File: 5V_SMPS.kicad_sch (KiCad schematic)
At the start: 13 parts, among them U3 TS30041

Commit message: V3 2. Update ready for check
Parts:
- renumbered C5 to C44, C6 to C45, C15 to C46, C16 to C47, C17 to C48, D7 to D16, L1 to L3, R17 to R43, R18 to R44, R19 to R45, R20 to R46, R21 to R47, U3 to U13
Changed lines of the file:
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@@
   (symbol (lib_id "Device:R_Small") (at 202.565 75.565 0)
     (in_bom yes) (on_board yes)
-    (property "Reference" "R21" (id 0) (at 203.835 74.295 0)
+    (property "Reference" "R47" (id 0) (at 203.835 74.295 0)
       (effects (font (size 1.27 1.27)) (justify left))
     )
@@
   (symbol (lib_id "Device:C") (at 111.76 72.39 180)
     (in_bom yes) (on_board yes)
-    (property "Reference" "C5" (id 0) (at 114.3 69.85 0))
+    (property "Reference" "C44" (id 0) (at 114.3 69.85 0))
     (property "Value" "22u" (id 1) (at 114.3 74.93 0))
     (property "Footprint" "Capacitor_SMD:C_0805_2012Metric" (id 2) (at 110.7948 68.58 0)
@@
   (symbol (lib_id "Device:L") (at 170.815 57.785 90)
     (in_bom yes) (on_board yes)
-    (property "Reference" "L1" (id 0) (at 170.815 52.959 90))
+    (property "Reference" "L3" (id 0) (at 170.815 52.959 90))
     (property "Value" "4.7u" (id 1) (at 170.815 55.2704 90))
     (property "Footprint" "TXV_Library_Footprints:SRN4018TA-4R7M" (id 2) (at 170.815 57.785 0)
@@
   (symbol (lib_id "Device:C") (at 187.325 75.565 180)
     (in_bom yes) (on_board yes)
-    (property "Reference" "C17" (id 0) (at 189.865 73.025 0))
+    (property "Reference" "C48" (id 0) (at 189.865 73.025 0))
     (property "Value" "22u" (id 1) (at 188.595 78.105 0))
     (property "Footprint" "Capacitor_SMD:C_0805_2012Metric" (id 2) (at 186.3598 71.755 0)
@@
   (symbol (lib_id "Device:LED_Small_Filled") (at 194.31 75.565 90)
     (in_bom yes) (on_board yes)
-    (property "Reference" "D7" (id 0) (at 196.85 74.295 90))
+    (property "Reference" "D16" (id 0) (at 196.85 74.295 90))
     (property "Value" "5V" (id 1) (at 196.85 76.835 90))
     (property "Footprint" "LED_SMD:LED_0603_1608Metric" (id 2) (at 194.31 75.565 90)
@@
   (symbol (lib_id "Device:C") (at 180.975 75.565 180)
     (in_bom yes) (on_board yes)
-    (property "Reference" "C16" (id 0) (at 183.515 73.025 0))
+    (property "Reference" "C47" (id 0) (at 183.515 73.025 0))
     (property "Value" "22u" (id 1) (at 182.88 78.105 0))
     (property "Footprint" "Capacitor_SMD:C_0805_2012Metric" (id 2) (at 180.0098 71.755 0)
@@
   (symbol (lib_id "Device:R_Small") (at 194.31 66.675 0)
     (in_bom yes) (on_board yes)
-    (property "Reference" "R19" (id 0) (at 199.39 65.405 0)
+    (property "Reference" "R45" (id 0) (at 199.39 65.405 0)
       (effects (font (size 1.27 1.27)) (justify right))
     )
@@
   (symbol (lib_id "Device:R") (at 175.895 80.645 0)
     (in_bom yes) (on_board yes)
-    (property "Reference" "R18" (id 0) (at 170.815 80.01 0)
+    (property "Reference" "R44" (id 0) (at 170.815 80.01 0)
       (effects (font (size 1.27 1.27)) (justify left))
     )
@@
   (symbol (lib_id "Device:R_Small") (at 202.565 66.675 0)
     (in_bom yes) (on_board yes)
-    (property "Reference" "R20" (id 0) (at 203.835 65.405 0)
+    (property "Reference" "R46" (id 0) (at 203.835 65.405 0)
       (effects (font (size 1.27 1.27)) (justify left))
     )
@@
   (symbol (lib_id "Device:R") (at 175.895 69.215 180)
     (in_bom yes) (on_board yes)
-    (property "Reference" "R17" (id 0) (at 172.72 68.58 0))
+    (property "Reference" "R43" (id 0) (at 172.72 68.58 0))
     (property "Value" "R" (id 1) (at 175.895 67.945 90))
     (property "Footprint" "Resistor_SMD:R_0603_1608Metric" (id 2) (at 177.673 69.215 90)
@@
   (symbol (lib_id "TXV_Library_Symbols:TS30041") (at 140.335 69.215 0)
     (in_bom yes) (on_board yes)
-    (property "Reference" "U3" (id 0) (at 140.335 51.054 0))
+    (property "Reference" "U13" (id 0) (at 140.335 51.054 0))
     (property "Value" "TS30041" (id 1) (at 140.335 53.3654 0))
     (property "Footprint" "Package_DFN_QFN:QFN-16-1EP_3x3mm_P0.5mm_EP1.75x1.75mm_ThermalVias" (id 2) (at 139.065 98.425 0)
@@
   (symbol (lib_id "Device:C") (at 160.655 57.785 270)
     (in_bom yes) (on_board yes)
-    (property "Reference" "C15" (id 0) (at 160.655 51.3842 90))
+    (property "Reference" "C46" (id 0) (at 160.655 51.3842 90))
     (property "Value" "100n" (id 1) (at 160.655 53.6956 90))
     (property "Footprint" "Capacitor_SMD:C_0402_1005Metric" (id 2) (at 156.845 58.7502 0)
@@
   (symbol (lib_id "Device:C") (at 118.745 72.39 0)
     (in_bom yes) (on_board yes)
-    (property "Reference" "C6" (id 0) (at 121.285 69.85 0))
+    (property "Reference" "C45" (id 0) (at 121.285 69.85 0))
     (property "Value" "100n" (id 1) (at 121.92 74.93 0))
     (property "Footprint" "Capacitor_SMD:C_0402_1005Metric" (id 2) (at 119.7102 76.2 0)

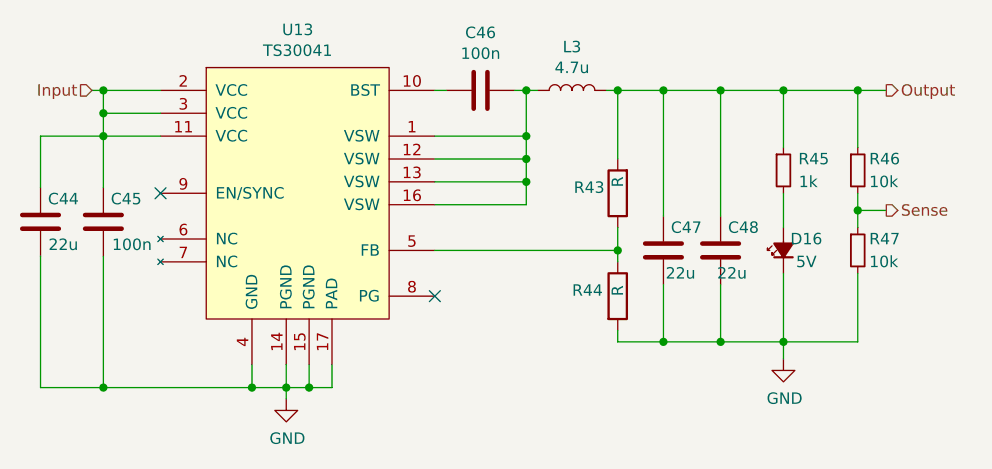
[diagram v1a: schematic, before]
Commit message: Schematic: Changed Polarity of umbilical connectors Schematic: Added TVS diode to battery_sense Schematic: Some minor prettyfication
Still wrong: Main LiIon Charger Enable connect to STM32
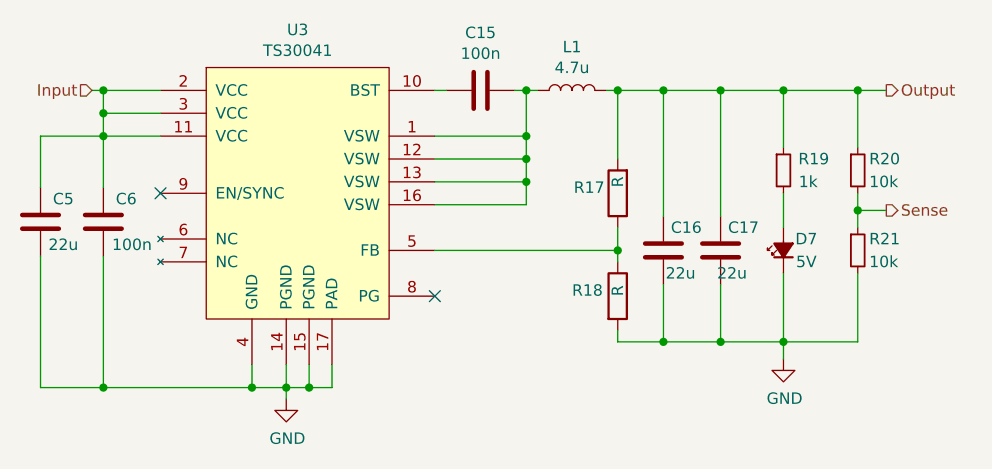
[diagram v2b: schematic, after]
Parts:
- renumbered C46 to C15, C47 to C16, C48 to C17, C44 to C5, C45 to C6, D16 to D7, L3 to L1, R43 to R17, R44 to R18, R45 to R19, R46 to R20, R47 to R21, U13 to U3
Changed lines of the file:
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@@
     (effects (font (size 1.27 1.27)) (justify right))
   )
-  (symbol (lib_id "Device:R_Small") (at 202.565 75.565 0)
-    (in_bom yes) (on_board yes)
-    (property "Reference" "R47" (id 0) (at 203.835 74.295 0)
+  (symbol (lib_id "Device:R_Small") (at 202.565 75.565 0) (unit 1)
+    (in_bom yes) (on_board yes)
+    (property "Reference" "R21" (id 0) (at 203.835 74.295 0)
       (effects (font (size 1.27 1.27)) (justify left))
     )
@@
     (pin "2")
   )
-  (symbol (lib_id "Device:C") (at 111.76 72.39 180)
-    (in_bom yes) (on_board yes)
-    (property "Reference" "C44" (id 0) (at 114.3 69.85 0))
+  (symbol (lib_id "Device:C") (at 111.76 72.39 180) (unit 1)
+    (in_bom yes) (on_board yes)
+    (property "Reference" "C5" (id 0) (at 114.3 69.85 0))
     (property "Value" "22u" (id 1) (at 114.3 74.93 0))
     (property "Footprint" "Capacitor_SMD:C_0805_2012Metric" (id 2) (at 110.7948 68.58 0)
@@
     (pin "2")
   )
-  (symbol (lib_id "Device:L") (at 170.815 57.785 90)
-    (in_bom yes) (on_board yes)
-    (property "Reference" "L3" (id 0) (at 170.815 52.959 90))
+  (symbol (lib_id "Device:L") (at 170.815 57.785 90) (unit 1)
+    (in_bom yes) (on_board yes)
+    (property "Reference" "L1" (id 0) (at 170.815 52.959 90))
     (property "Value" "4.7u" (id 1) (at 170.815 55.2704 90))
     (property "Footprint" "TXV_Library_Footprints:SRN4018TA-4R7M" (id 2) (at 170.815 57.785 0)
@@
     (pin "2")
   )
-  (symbol (lib_id "Device:C") (at 187.325 75.565 180)
-    (in_bom yes) (on_board yes)
-    (property "Reference" "C48" (id 0) (at 189.865 73.025 0))
+  (symbol (lib_id "Device:C") (at 187.325 75.565 180) (unit 1)
+    (in_bom yes) (on_board yes)
+    (property "Reference" "C17" (id 0) (at 189.865 73.025 0))
     (property "Value" "22u" (id 1) (at 188.595 78.105 0))
     (property "Footprint" "Capacitor_SMD:C_0805_2012Metric" (id 2) (at 186.3598 71.755 0)
@@
     (pin "2")
   )
-  (symbol (lib_id "Device:LED_Small_Filled") (at 194.31 75.565 90)
-    (in_bom yes) (on_board yes)
-    (property "Reference" "D16" (id 0) (at 196.85 74.295 90))
+  (symbol (lib_id "Device:LED_Small_Filled") (at 194.31 75.565 90) (unit 1)
+    (in_bom yes) (on_board yes)
+    (property "Reference" "D7" (id 0) (at 196.85 74.295 90))
     (property "Value" "5V" (id 1) (at 196.85 76.835 90))
     (property "Footprint" "LED_SMD:LED_0603_1608Metric" (id 2) (at 194.31 75.565 90)
@@
     (pin "2")
   )
-  (symbol (lib_id "power:GND") (at 139.065 92.075 0)
-    (in_bom yes) (on_board yes)
-    (property "Reference" "#PWR0102" (id 0) (at 139.065 98.425 0)
+  (symbol (lib_id "power:GND") (at 139.065 92.075 0) (unit 1)
+    (in_bom yes) (on_board yes)
+    (property "Reference" "#PWR093" (id 0) (at 139.065 98.425 0)
       (effects (font (size 1.27 1.27)) hide)
     )
@@
     (pin "1")
   )
-  (symbol (lib_id "Device:C") (at 180.975 75.565 180)
-    (in_bom yes) (on_board yes)
-    (property "Reference" "C47" (id 0) (at 183.515 73.025 0))
+  (symbol (lib_id "Device:C") (at 180.975 75.565 180) (unit 1)
+    (in_bom yes) (on_board yes)
+    (property "Reference" "C16" (id 0) (at 183.515 73.025 0))
     (property "Value" "22u" (id 1) (at 182.88 78.105 0))
     (property "Footprint" "Capacitor_SMD:C_0805_2012Metric" (id 2) (at 180.0098 71.755 0)
@@
     (pin "2")
   )
-  (symbol (lib_id "Device:R_Small") (at 194.31 66.675 0)
-    (in_bom yes) (on_board yes)
-    (property "Reference" "R45" (id 0) (at 199.39 65.405 0)
+  (symbol (lib_id "Device:R_Small") (at 194.31 66.675 0) (unit 1)
+    (in_bom yes) (on_board yes)
+    (property "Reference" "R19" (id 0) (at 199.39 65.405 0)
       (effects (font (size 1.27 1.27)) (justify right))
     )
@@
     (pin "2")
   )
-  (symbol (lib_id "power:GND") (at 194.31 87.63 0)
-    (in_bom yes) (on_board yes)
-    (property "Reference" "#PWR0103" (id 0) (at 194.31 93.98 0)
+  (symbol (lib_id "power:GND") (at 194.31 87.63 0) (unit 1)
+    (in_bom yes) (on_board yes)
+    (property "Reference" "#PWR0101" (id 0) (at 194.31 93.98 0)
       (effects (font (size 1.27 1.27)) hide)
     )
@@
     (pin "1")
   )
-  (symbol (lib_id "Device:R") (at 175.895 80.645 0)
-    (in_bom yes) (on_board yes)
-    (property "Reference" "R44" (id 0) (at 170.815 80.01 0)
+  (symbol (lib_id "Device:R") (at 175.895 80.645 0) (unit 1)
+    (in_bom yes) (on_board yes)
+    (property "Reference" "R18" (id 0) (at 170.815 80.01 0)
       (effects (font (size 1.27 1.27)) (justify left))
     )
@@
     (pin "2")
   )
-  (symbol (lib_id "Device:R_Small") (at 202.565 66.675 0)
-    (in_bom yes) (on_board yes)
-    (property "Reference" "R46" (id 0) (at 203.835 65.405 0)
+  (symbol (lib_id "Device:R_Small") (at 202.565 66.675 0) (unit 1)
+    (in_bom yes) (on_board yes)
+    (property "Reference" "R20" (id 0) (at 203.835 65.405 0)
       (effects (font (size 1.27 1.27)) (justify left))
     )
@@
     (pin "2")
   )
-  (symbol (lib_id "Device:R") (at 175.895 69.215 180)
-    (in_bom yes) (on_board yes)
-    (property "Reference" "R43" (id 0) (at 172.72 68.58 0))
+  (symbol (lib_id "Device:R") (at 175.895 69.215 180) (unit 1)
+    (in_bom yes) (on_board yes)
+    (property "Reference" "R17" (id 0) (at 172.72 68.58 0))
     (property "Value" "R" (id 1) (at 175.895 67.945 90))
     (property "Footprint" "Resistor_SMD:R_0603_1608Metric" (id 2) (at 177.673 69.215 90)
@@
     (pin "2")
   )
-  (symbol (lib_id "TXV_Library_Symbols:TS30041") (at 140.335 69.215 0)
-    (in_bom yes) (on_board yes)
-    (property "Reference" "U13" (id 0) (at 140.335 51.054 0))
+  (symbol (lib_id "TXV_Library_Symbols:TS30041") (at 140.335 69.215 0) (unit 1)
+    (in_bom yes) (on_board yes)
+    (property "Reference" "U3" (id 0) (at 140.335 51.054 0))
     (property "Value" "TS30041" (id 1) (at 140.335 53.3654 0))
     (property "Footprint" "Package_DFN_QFN:QFN-16-1EP_3x3mm_P0.5mm_EP1.75x1.75mm_ThermalVias" (id 2) (at 139.065 98.425 0)
@@
     (pin "9")
   )
-  (symbol (lib_id "Device:C") (at 160.655 57.785 270)
-    (in_bom yes) (on_board yes)
-    (property "Reference" "C46" (id 0) (at 160.655 51.3842 90))
+  (symbol (lib_id "Device:C") (at 160.655 57.785 270) (unit 1)
+    (in_bom yes) (on_board yes)
+    (property "Reference" "C15" (id 0) (at 160.655 51.3842 90))
     (property "Value" "100n" (id 1) (at 160.655 53.6956 90))
     (property "Footprint" "Capacitor_SMD:C_0402_1005Metric" (id 2) (at 156.845 58.7502 0)
@@
     (pin "2")
   )
-  (symbol (lib_id "Device:C") (at 118.745 72.39 0)
-    (in_bom yes) (on_board yes)
-    (property "Reference" "C45" (id 0) (at 121.285 69.85 0))
+  (symbol (lib_id "Device:C") (at 118.745 72.39 0) (unit 1)
+    (in_bom yes) (on_board yes)
+    (property "Reference" "C6" (id 0) (at 121.285 69.85 0))
     (property "Value" "100n" (id 1) (at 121.92 74.93 0))
     (property "Footprint" "Capacitor_SMD:C_0402_1005Metric" (id 2) (at 119.7102 76.2 0)

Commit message: Revert "PMU V3 "ready to order?""
This reverts commit e5aaef69110c3557dfda333950fee24891806424.
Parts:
- renumbered C5 to C44, C6 to C45, C15 to C46, C16 to C47, C17 to C48, D7 to D16, L1 to L3, R17 to R43, R18 to R44, R19 to R45, R20 to R46, R21 to R47, U3 to U13
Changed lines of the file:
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@@
     (effects (font (size 1.27 1.27)) (justify right))
   )
-  (symbol (lib_id "Device:R_Small") (at 202.565 75.565 0) (unit 1)
-    (in_bom yes) (on_board yes)
-    (property "Reference" "R21" (id 0) (at 203.835 74.295 0)
+  (symbol (lib_id "Device:R_Small") (at 202.565 75.565 0)
+    (in_bom yes) (on_board yes)
+    (property "Reference" "R47" (id 0) (at 203.835 74.295 0)
       (effects (font (size 1.27 1.27)) (justify left))
     )
@@
     (pin "2")
   )
-  (symbol (lib_id "Device:C") (at 111.76 72.39 180) (unit 1)
-    (in_bom yes) (on_board yes)
-    (property "Reference" "C5" (id 0) (at 114.3 69.85 0))
+  (symbol (lib_id "Device:C") (at 111.76 72.39 180)
+    (in_bom yes) (on_board yes)
+    (property "Reference" "C44" (id 0) (at 114.3 69.85 0))
     (property "Value" "22u" (id 1) (at 114.3 74.93 0))
     (property "Footprint" "Capacitor_SMD:C_0805_2012Metric" (id 2) (at 110.7948 68.58 0)
@@
     (pin "2")
   )
-  (symbol (lib_id "Device:L") (at 170.815 57.785 90) (unit 1)
-    (in_bom yes) (on_board yes)
-    (property "Reference" "L1" (id 0) (at 170.815 52.959 90))
+  (symbol (lib_id "Device:L") (at 170.815 57.785 90)
+    (in_bom yes) (on_board yes)
+    (property "Reference" "L3" (id 0) (at 170.815 52.959 90))
     (property "Value" "4.7u" (id 1) (at 170.815 55.2704 90))
     (property "Footprint" "TXV_Library_Footprints:SRN4018TA-4R7M" (id 2) (at 170.815 57.785 0)
@@
     (pin "2")
   )
-  (symbol (lib_id "Device:C") (at 187.325 75.565 180) (unit 1)
-    (in_bom yes) (on_board yes)
-    (property "Reference" "C17" (id 0) (at 189.865 73.025 0))
+  (symbol (lib_id "Device:C") (at 187.325 75.565 180)
+    (in_bom yes) (on_board yes)
+    (property "Reference" "C48" (id 0) (at 189.865 73.025 0))
     (property "Value" "22u" (id 1) (at 188.595 78.105 0))
     (property "Footprint" "Capacitor_SMD:C_0805_2012Metric" (id 2) (at 186.3598 71.755 0)
@@
     (pin "2")
   )
-  (symbol (lib_id "Device:LED_Small_Filled") (at 194.31 75.565 90) (unit 1)
-    (in_bom yes) (on_board yes)
-    (property "Reference" "D7" (id 0) (at 196.85 74.295 90))
+  (symbol (lib_id "Device:LED_Small_Filled") (at 194.31 75.565 90)
+    (in_bom yes) (on_board yes)
+    (property "Reference" "D16" (id 0) (at 196.85 74.295 90))
     (property "Value" "5V" (id 1) (at 196.85 76.835 90))
     (property "Footprint" "LED_SMD:LED_0603_1608Metric" (id 2) (at 194.31 75.565 90)
@@
     (pin "2")
   )
-  (symbol (lib_id "power:GND") (at 139.065 92.075 0) (unit 1)
-    (in_bom yes) (on_board yes)
-    (property "Reference" "#PWR093" (id 0) (at 139.065 98.425 0)
+  (symbol (lib_id "power:GND") (at 139.065 92.075 0)
+    (in_bom yes) (on_board yes)
+    (property "Reference" "#PWR0102" (id 0) (at 139.065 98.425 0)
       (effects (font (size 1.27 1.27)) hide)
     )
@@
     (pin "1")
   )
-  (symbol (lib_id "Device:C") (at 180.975 75.565 180) (unit 1)
-    (in_bom yes) (on_board yes)
-    (property "Reference" "C16" (id 0) (at 183.515 73.025 0))
+  (symbol (lib_id "Device:C") (at 180.975 75.565 180)
+    (in_bom yes) (on_board yes)
+    (property "Reference" "C47" (id 0) (at 183.515 73.025 0))
     (property "Value" "22u" (id 1) (at 182.88 78.105 0))
     (property "Footprint" "Capacitor_SMD:C_0805_2012Metric" (id 2) (at 180.0098 71.755 0)
@@
     (pin "2")
   )
-  (symbol (lib_id "Device:R_Small") (at 194.31 66.675 0) (unit 1)
-    (in_bom yes) (on_board yes)
-    (property "Reference" "R19" (id 0) (at 199.39 65.405 0)
+  (symbol (lib_id "Device:R_Small") (at 194.31 66.675 0)
+    (in_bom yes) (on_board yes)
+    (property "Reference" "R45" (id 0) (at 199.39 65.405 0)
       (effects (font (size 1.27 1.27)) (justify right))
     )
@@
     (pin "2")
   )
-  (symbol (lib_id "power:GND") (at 194.31 87.63 0) (unit 1)
-    (in_bom yes) (on_board yes)
-    (property "Reference" "#PWR0101" (id 0) (at 194.31 93.98 0)
+  (symbol (lib_id "power:GND") (at 194.31 87.63 0)
+    (in_bom yes) (on_board yes)
+    (property "Reference" "#PWR0103" (id 0) (at 194.31 93.98 0)
       (effects (font (size 1.27 1.27)) hide)
     )
@@
     (pin "1")
   )
-  (symbol (lib_id "Device:R") (at 175.895 80.645 0) (unit 1)
-    (in_bom yes) (on_board yes)
-    (property "Reference" "R18" (id 0) (at 170.815 80.01 0)
+  (symbol (lib_id "Device:R") (at 175.895 80.645 0)
+    (in_bom yes) (on_board yes)
+    (property "Reference" "R44" (id 0) (at 170.815 80.01 0)
       (effects (font (size 1.27 1.27)) (justify left))
     )
@@
     (pin "2")
   )
-  (symbol (lib_id "Device:R_Small") (at 202.565 66.675 0) (unit 1)
-    (in_bom yes) (on_board yes)
-    (property "Reference" "R20" (id 0) (at 203.835 65.405 0)
+  (symbol (lib_id "Device:R_Small") (at 202.565 66.675 0)
+    (in_bom yes) (on_board yes)
+    (property "Reference" "R46" (id 0) (at 203.835 65.405 0)
       (effects (font (size 1.27 1.27)) (justify left))
     )
@@
     (pin "2")
   )
-  (symbol (lib_id "Device:R") (at 175.895 69.215 180) (unit 1)
-    (in_bom yes) (on_board yes)
-    (property "Reference" "R17" (id 0) (at 172.72 68.58 0))
+  (symbol (lib_id "Device:R") (at 175.895 69.215 180)
+    (in_bom yes) (on_board yes)
+    (property "Reference" "R43" (id 0) (at 172.72 68.58 0))
     (property "Value" "R" (id 1) (at 175.895 67.945 90))
     (property "Footprint" "Resistor_SMD:R_0603_1608Metric" (id 2) (at 177.673 69.215 90)
@@
     (pin "2")
   )
-  (symbol (lib_id "TXV_Library_Symbols:TS30041") (at 140.335 69.215 0) (unit 1)
-    (in_bom yes) (on_board yes)
-    (property "Reference" "U3" (id 0) (at 140.335 51.054 0))
+  (symbol (lib_id "TXV_Library_Symbols:TS30041") (at 140.335 69.215 0)
+    (in_bom yes) (on_board yes)
+    (property "Reference" "U13" (id 0) (at 140.335 51.054 0))
     (property "Value" "TS30041" (id 1) (at 140.335 53.3654 0))
     (property "Footprint" "Package_DFN_QFN:QFN-16-1EP_3x3mm_P0.5mm_EP1.75x1.75mm_ThermalVias" (id 2) (at 139.065 98.425 0)
@@
     (pin "9")
   )
-  (symbol (lib_id "Device:C") (at 160.655 57.785 270) (unit 1)
-    (in_bom yes) (on_board yes)
-    (property "Reference" "C15" (id 0) (at 160.655 51.3842 90))
+  (symbol (lib_id "Device:C") (at 160.655 57.785 270)
+    (in_bom yes) (on_board yes)
+    (property "Reference" "C46" (id 0) (at 160.655 51.3842 90))
     (property "Value" "100n" (id 1) (at 160.655 53.6956 90))
     (property "Footprint" "Capacitor_SMD:C_0402_1005Metric" (id 2) (at 156.845 58.7502 0)
@@
     (pin "2")
   )
-  (symbol (lib_id "Device:C") (at 118.745 72.39 0) (unit 1)
-    (in_bom yes) (on_board yes)
-    (property "Reference" "C6" (id 0) (at 121.285 69.85 0))
+  (symbol (lib_id "Device:C") (at 118.745 72.39 0)
+    (in_bom yes) (on_board yes)
+    (property "Reference" "C45" (id 0) (at 121.285 69.85 0))
     (property "Value" "100n" (id 1) (at 121.92 74.93 0))
     (property "Footprint" "Capacitor_SMD:C_0402_1005Metric" (id 2) (at 119.7102 76.2 0)
